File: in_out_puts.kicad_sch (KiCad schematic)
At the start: 16 parts, among them J2 Status_leds, J3 Dome, J5 Motor1, J6 Motor2, J7 Speaker, Q4 PNP, Q5 NMOS, Q6 NMOS, SW2 SW_Push, SW3 SW_Push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

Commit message: simulated IR-constant-current circuit, worked on schematic
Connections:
- net IO42: now reaches Q6.2 (G)
- net IO41: now reaches Q5.2 (G)
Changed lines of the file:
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@@
+		)
+	)
+	(global_label "IO41"
+		(shape input)
+		(at 35.56 127 180)
+		(fields_autoplaced yes)
+		(effects
+			(font
+				(size 1.27 1.27)
+			)
+			(justify right)
+		)
+		(property "Intersheetrefs" "${INTERSHEET_REFS}"
+			(at 28.2205 127 0)
+			(effects
+				(font
+					(size 1.27 1.27)
+				)
+				(justify right)
+				(hide yes)
+			)
 		)
 	)
@@
 			(effects
 				(font
+					(size 1.27 1.27)
+				)
+				(justify right)
+				(hide yes)
+			)
+		)
+	)
+	(global_label "IO42"
+		(shape input)
+		(at 64.77 127 180)
+		(fields_autoplaced yes)
+		(effects
+			(font
+				(size 1.27 1.27)
+			)
+			(justify right)
+		)
+		(property "Intersheetrefs" "${INTERSHEET_REFS}"
+			(at 57.4305 127 0)
+			(effects
+				(font

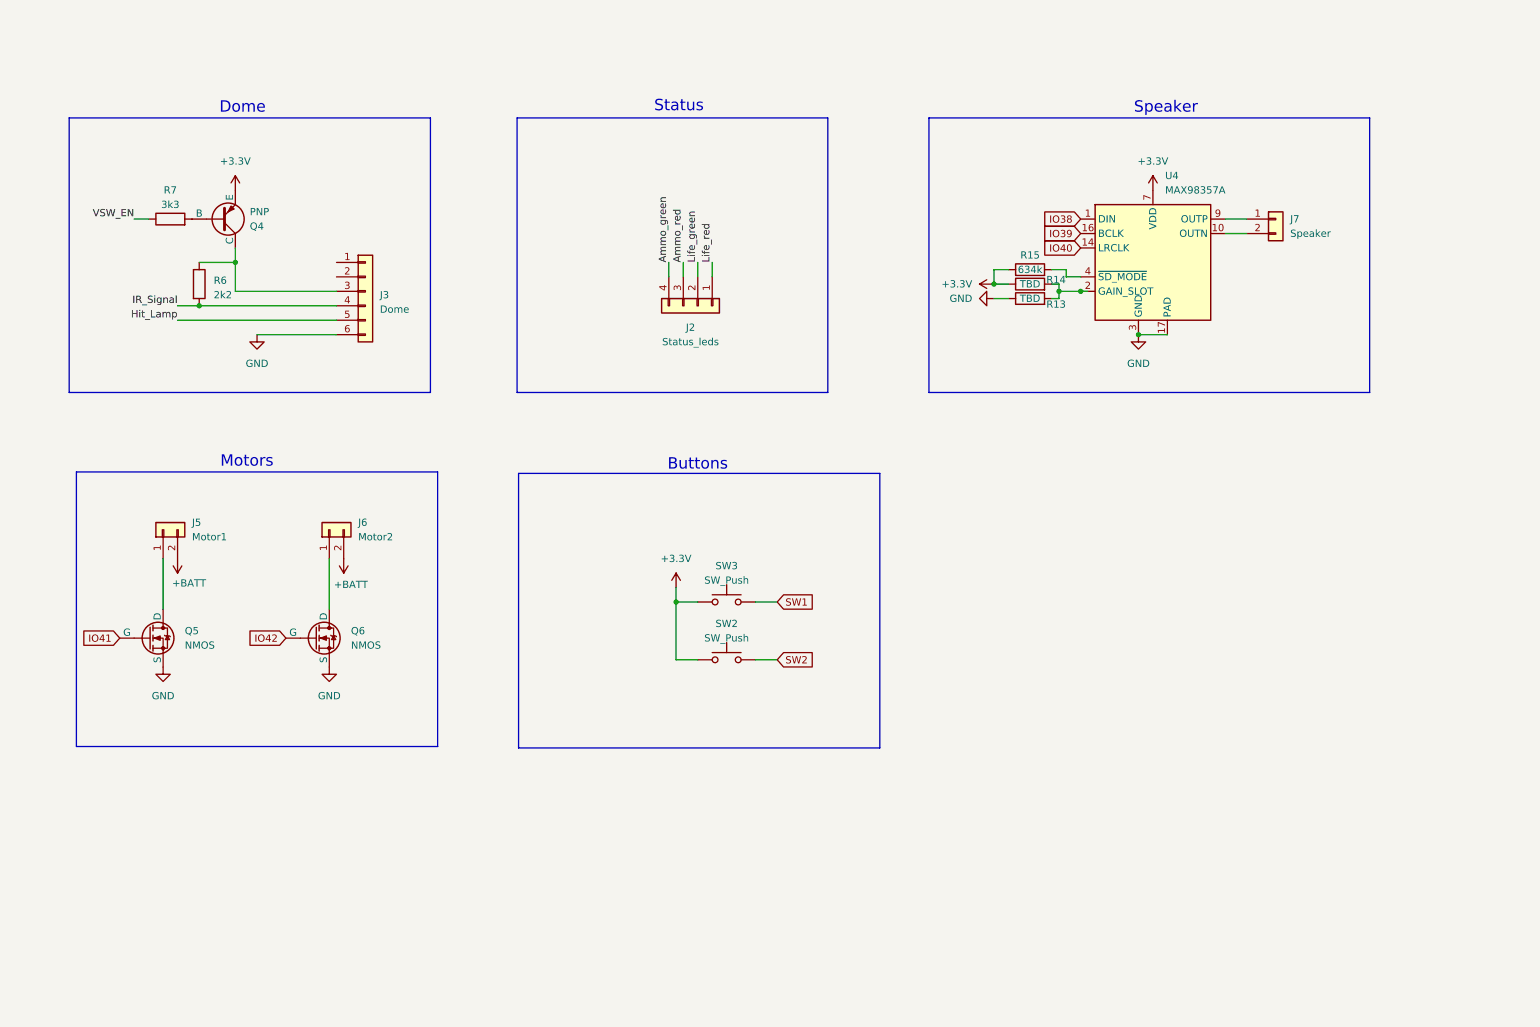
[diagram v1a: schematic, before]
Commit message: prepared for jlcpcb ordering.
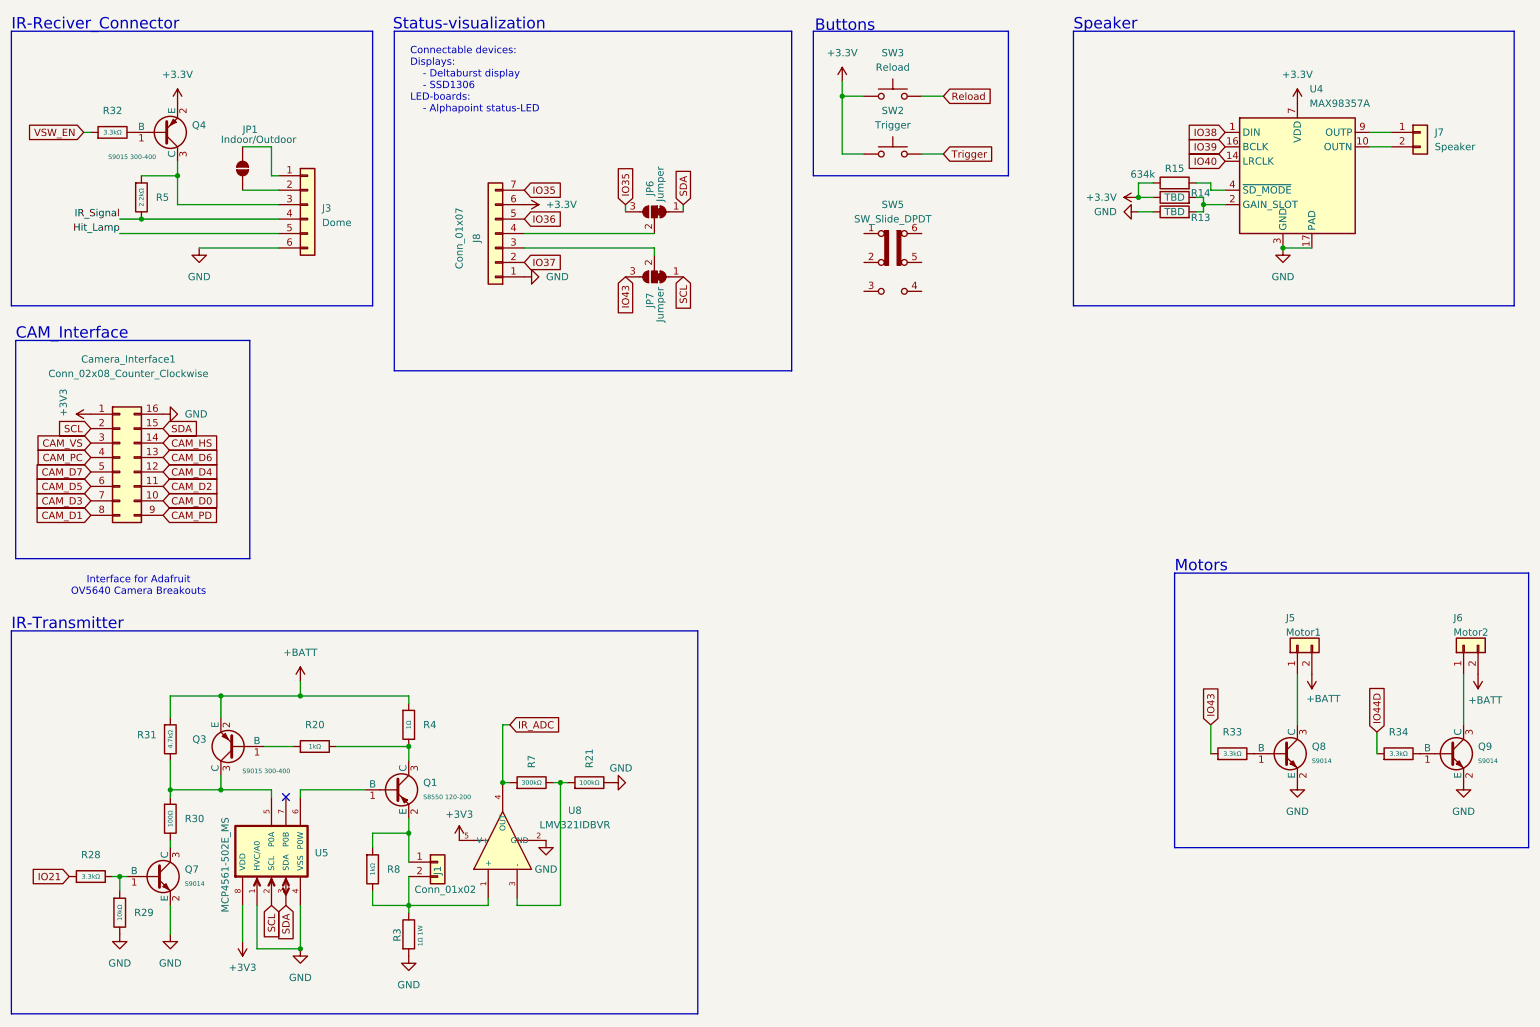
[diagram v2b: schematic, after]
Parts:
- removed J2: Status_leds, symbol Connector_Generic:Conn_01x04
- removed Q4: PNP, symbol Simulation_SPICE:PNP
- removed Q5, Q6: NMOS, symbol Simulation_SPICE:NMOS
- removed R6: 2k2, symbol Device:R
- removed R7: 3k3, symbol Device:R
- added Camera_Interface1: Conn_02x08_Counter_Clockwise, symbol Connector_Generic:Conn_02x08_Counter_Clockwise
- added J1: Conn_01x02, symbol Connector_Generic:Conn_01x02
- added J8: Conn_01x07, symbol Connector_Generic:Conn_01x07
- added JP1: Indoor/Outdoor, symbol Jumper:SolderJumper_2_Open
- added JP6, JP7: Jumper, symbol Jumper:SolderJumper_3_Bridged12
- added Q1: S8550 120-200, PCM_JLCPCB:Q_SOT-23, symbol PCM_JLCPCB-Transistors:PNP,S8550 120-200
- added Q3, Q4: S9015 300-400, PCM_JLCPCB:Q_SOT-23, symbol PCM_JLCPCB-Transistors:PNP,S9015 300-400
- added Q7, Q8, Q9: S9014, PCM_JLCPCB:Q_SOT-23, symbol PCM_JLCPCB-Transistors:NPN,S9014
- added R20, R8: 1kΩ, PCM_JLCPCB:R_0603, symbol PCM_JLCPCB-Resistors:0603,1kΩ
- added R21: 100kΩ, PCM_JLCPCB:R_0603, symbol PCM_JLCPCB-Resistors:0603,100kΩ
- added R28, R32, R33, R34: 3.3kΩ, PCM_JLCPCB:R_0603, symbol PCM_JLCPCB-Resistors:0603,3.3kΩ
- added R29: 10kΩ, PCM_JLCPCB:R_0603, symbol PCM_JLCPCB-Resistors:0603,10kΩ
- added R3: 1Ω 1W, symbol Device:R
- added R30: 100Ω, PCM_JLCPCB:R_0603, symbol PCM_JLCPCB-Resistors:0603,100Ω
- added R31: 4.7kΩ, PCM_JLCPCB:R_0603, symbol PCM_JLCPCB-Resistors:0603,4.7kΩ
- added R4: 1Ω, PCM_JLCPCB:R_0603, symbol PCM_JLCPCB-Resistors:0603,1Ω
- added R5: 2.2kΩ, PCM_JLCPCB:R_0603, symbol PCM_JLCPCB-Resistors:0603,2.2kΩ
- added R7: 300kΩ, PCM_JLCPCB:R_0603, symbol PCM_JLCPCB-Resistors:0603,300kΩ
- added SW5: SW_Slide_DPDT, symbol Switch:SW_Slide_DPDT
- added U5: MCP4561-502E_MS, MCP4561-502E_MS:SOP65P490X110-8N, symbol MCP4561-502E_MS:MCP4561-502E_MS
- added U8: LMV321IDBVR, PCM_JLCPCB:SOT-23-5_L3.0-W1.7-P0.95-LS2.8-BR, symbol PCM_JLCPCB-Analog:Op-Amp, LMV321IDBVR
- SW2: value SW_Push -> Trigger
- SW3: value SW_Push -> Reload
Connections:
- net +3.3V: now also J8.6 (Pin_6), Q4.2 (E)
- net +BATT: now also Q3.2 (E), R31.1, R4.1
- net GND: now also Camera_Interface1.16 (Pin_16), J8.1 (Pin_1), Q7.2 (E), Q8.2 (E), Q9.2 (E), R21.2, R29.2, R3.2, U5.1 (HVC/A0), U5.4 (VSS), U8.2 (GND)
- net IR_Signal: now also R5.2
- net VSW_EN: now also R32.1
- net at J6.1 (Pin_1): now also Q9.3 (C)
- net at J5.1 (Pin_1): now also Q8.3 (C)
- net at J3.3 (Pin_3): now also Q4.3 (C), R5.1
- net at J3.1 (Pin_1): now also JP1.2 (B)
- net at J3.2 (Pin_2): now also JP1.1 (A)
- net SW1 renamed Reload
- net SW2 renamed Trigger
- new net: J1.2 (Pin_2), R3.1, R8.2, U8.1 (+)
- new net: Q7.1 (B), R28.2, R29.1
- new net: J8.3 (Pin_3), JP7.2 (C)
- new net: Q9.1 (B), R34.2
- new net: Q3.1 (B), R20.1
- new net: Q3.3 (C), R30.1, R31.2, U5.5 (P0A)
- new net: Q8.1 (B), R33.2
- new net: J1.1 (Pin_1), Q1.2 (E), R8.1
- new net: R21.1, R7.2, U8.3 (-)
- new net: J8.4 (Pin_4), JP6.2 (C)
- new net: Q1.1 (B), U5.6 (P0W)
- new net: Q1.3 (C), R20.2, R4.2
- new net: Q7.3 (C), R30.2
- new net: Q4.1 (B), R32.2
- new net +3V3: Camera_Interface1.1 (Pin_1), U5.8 (VDD), U8.5 (V+)
- new net CAM_D0: Camera_Interface1.10 (Pin_10)
- new net CAM_D1: Camera_Interface1.8 (Pin_8)
- new net CAM_D2: Camera_Interface1.11 (Pin_11)
- new net CAM_D3: Camera_Interface1.7 (Pin_7)
- new net CAM_D4: Camera_Interface1.12 (Pin_12)
- new net CAM_D5: Camera_Interface1.6 (Pin_6)
- new net CAM_D6: Camera_Interface1.13 (Pin_13)
- new net CAM_D7: Camera_Interface1.5 (Pin_5)
- new net CAM_HS: Camera_Interface1.14 (Pin_14)
- new net CAM_PC: Camera_Interface1.4 (Pin_4)
- new net CAM_PD: Camera_Interface1.9 (Pin_9)
- new net CAM_VS: Camera_Interface1.3 (Pin_3)
- new net IO21: R28.1
- new net IO35: J8.7 (Pin_7), JP6.3 (B)
- new net IO36: J8.5 (Pin_5)
- new net IO37: J8.2 (Pin_2)
- new net IO43: JP7.3 (B), R33.1
- new net IO44D: R34.1
- new net IR_ADC: R7.1, U8.4 (OUT)
- new net SCL: Camera_Interface1.2 (Pin_2), JP7.1 (A), U5.2 (SCL)
- new net SDA: Camera_Interface1.15 (Pin_15), JP6.1 (A), U5.3 (SDA)
- no-connect marks 0 -> 1
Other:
- note added: "CAM_Interface"
- note added: "Connectable devices: Displays: - Deltaburst display - SSD1306 LED-boards: - Alphapoint status-LED"
- note added: "IR-Reciver_Connector"
- note added: "IR-Transmitter"
- note added: "Interface for Adafruit OV5640 Camera Breakouts"
- note added: "Status-visualization"
- note removed: "Dome"
- note removed: "Status"
- moved on the sheet: J3, J5, J6, J7, R13, R14, R15, SW2, SW3, U4

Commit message: checked and fixed schematic, analized it with traceformer.io ai
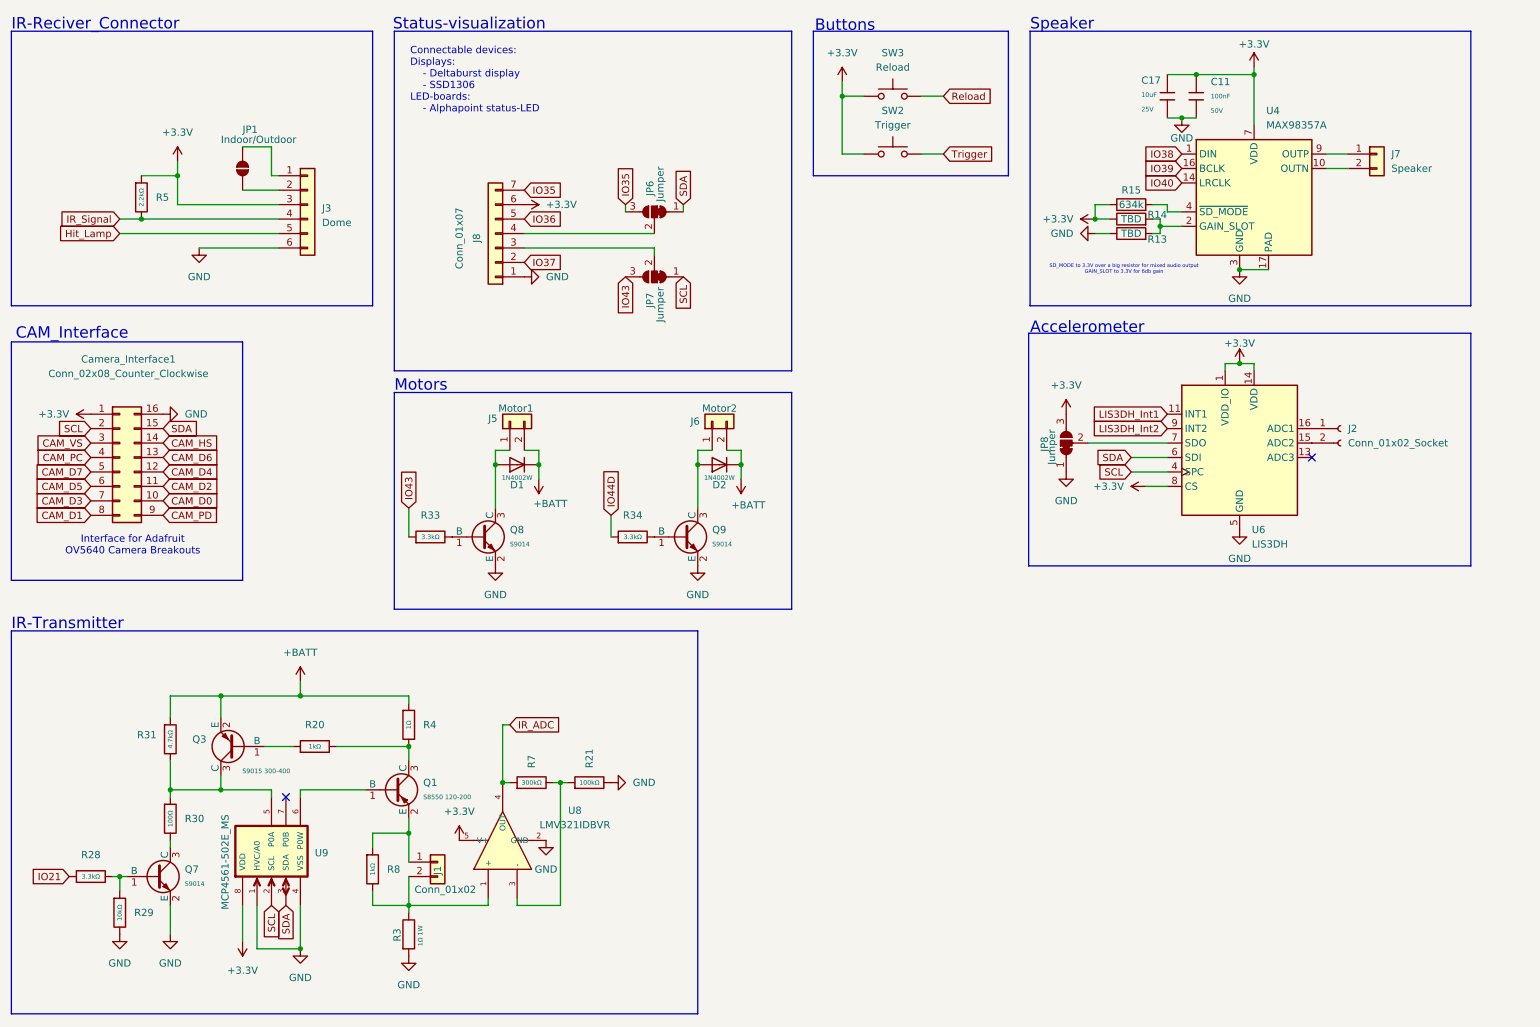
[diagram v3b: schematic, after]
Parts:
- removed Q4: S9015 300-400, PCM_JLCPCB:Q_SOT-23, symbol PCM_JLCPCB-Transistors:PNP,S9015 300-400
- removed R32: 3.3kΩ, PCM_JLCPCB:R_0603, symbol PCM_JLCPCB-Resistors:0603,3.3kΩ
- removed SW5: SW_Slide_DPDT, symbol Switch:SW_Slide_DPDT
- removed U5: MCP4561-502E_MS, MCP4561-502E_MS:SOP65P490X110-8N, symbol MCP4561-502E_MS:MCP4561-502E_MS
- added C11: 100nF, PCM_JLCPCB:C_0603, symbol PCM_JLCPCB-Capacitors:0603,100nF
- added C17: 10uF, PCM_JLCPCB:C_0805, symbol PCM_JLCPCB-Capacitors:0805,10uF
- added D1, D2: 1N4002W, PCM_JLCPCB:D_SOD-123FL, symbol PCM_JLCPCB-Diodes:General,1N4002W
- added J2: Conn_01x02_Socket, Connector_PinHeader_2.54mm:PinHeader_1x02_P2.54mm_Vertical, symbol Connector:Conn_01x02_Socket
- added JP8: Jumper, Jumper:SolderJumper-3_P1.3mm_Bridged12_RoundedPad1.0x1.5mm_NumberLabels, symbol Jumper:SolderJumper_3_Bridged12
- added U6: LIS3DH, Package_LGA:LGA-16_3x3mm_P0.5mm_LayoutBorder3x5y, symbol Sensor_Motion:LIS3DH
- added U9: MCP4561-502E_MS, MCP4561_502E_MS:SOP65P490X110-8N, symbol MCP4561-502E_MS:MCP4561-502E_MS
- Camera_Interface1: footprint (none) -> Connector_PinHeader_2.54mm:PinHeader_2x08_P2.54mm_Vertical
- J1: footprint (none) -> Connector_PinHeader_2.54mm:PinHeader_1x01_P2.54mm_Vertical
- J3: footprint (none) -> Connector_PinHeader_1.00mm:PinHeader_1x06_P1.00mm_Vertical
- J5, J6, J7: footprint (none) -> Connector_PinHeader_1.00mm:PinHeader_1x02_P1.00mm_Vertical
- J8: footprint (none) -> Connector_PinHeader_2.54mm:PinHeader_1x07_P2.54mm_Vertical
- JP1: footprint (none) -> Jumper:SolderJumper-2_P1.3mm_Open_RoundedPad1.0x1.5mm
- JP6, JP7: footprint (none) -> Jumper:SolderJumper-3_P1.3mm_Bridged12_RoundedPad1.0x1.5mm_NumberLabels
- R13, R14, R15: footprint (none) -> Resistor_SMD:R_0805_2012Metric_Pad1.20x1.40mm_HandSolder
- R3: footprint (none) -> Resistor_SMD:R_2512_6332Metric_Pad1.40x3.35mm_HandSolder
- SW2, SW3: footprint (none) -> Connector_PinHeader_1.00mm:PinHeader_1x02_P1.00mm_Horizontal
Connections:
- net +3V3 is gone; now on net +3.3V: Camera_Interface1.1 (Pin_1), U8.5 (V+)
- net +3.3V: now also J3.3 (Pin_3), R5.1, C11.1, C17.1, JP8.3 (B), U6.1 (VDD_IO), U6.14 (VDD), U6.8 (CS), U9.8 (VDD)
- net +BATT: now also D1.1, D2.1
- net GND: now also C11.2, C17.2, JP8.1 (A), U6.10 (GND), U6.12 (GND), U6.5 (GND), U9.1 (HVC/A0), U9.4 (VSS)
- net SCL: now also U6.4 (SPC), U9.2 (SCL)
- net SDA: now also U6.6 (SDI), U9.3 (SDA)
- net at J6.1 (Pin_1), Q9.3 (C): now also D2.2
- net at Q3.3 (C), R30.1, R31.2: now also U9.5 (P0A)
- net at J5.1 (Pin_1), Q8.3 (C): now also D1.2
- net at Q1.1 (B): now also U9.6 (P0W)
- new net: J2.1 (Pin_1), U6.16 (ADC1)
- new net: J2.2 (Pin_2), U6.15 (ADC2)
- new net: JP8.2 (C), U6.7 (SDO)
- new net LIS3DH_Int1: U6.11 (INT1)
- new net LIS3DH_Int2: U6.9 (INT2)
- no-connect marks 1 -> 2
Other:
- note added: "Accelerometer"
- note added: "SD_MODE to 3.3V over a big resistor for mixed audio output GAIN_SLOT to 3.3V for 6db gain"
- moved on the sheet: J5, J6, J7, Q8, Q9, R13, R14, R15, R33, R34, U4

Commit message: replaced ir-led constant current circuit
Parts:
- removed C11: 100nF, PCM_JLCPCB:C_0603, symbol PCM_JLCPCB-Capacitors:0603,100nF
- removed Q1: S8550 120-200, PCM_JLCPCB:Q_SOT-23, symbol PCM_JLCPCB-Transistors:PNP,S8550 120-200
- removed Q3: S9015 300-400, PCM_JLCPCB:Q_SOT-23, symbol PCM_JLCPCB-Transistors:PNP,S9015 300-400
- removed Q7: S9014, PCM_JLCPCB:Q_SOT-23, symbol PCM_JLCPCB-Transistors:NPN,S9014
- removed R20, R8: 1kΩ, PCM_JLCPCB:R_0603, symbol PCM_JLCPCB-Resistors:0603,1kΩ
- removed R21: 100kΩ, PCM_JLCPCB:R_0603, symbol PCM_JLCPCB-Resistors:0603,100kΩ
- removed R28, R33, R34: 3.3kΩ, PCM_JLCPCB:R_0603, symbol PCM_JLCPCB-Resistors:0603,3.3kΩ
- removed R29: 10kΩ, PCM_JLCPCB:R_0603, symbol PCM_JLCPCB-Resistors:0603,10kΩ
- removed R30: 100Ω, PCM_JLCPCB:R_0603, symbol PCM_JLCPCB-Resistors:0603,100Ω
- removed R31: 4.7kΩ, PCM_JLCPCB:R_0603, symbol PCM_JLCPCB-Resistors:0603,4.7kΩ
- removed R4: 1Ω, PCM_JLCPCB:R_0603, symbol PCM_JLCPCB-Resistors:0603,1Ω
- removed R5: 2.2kΩ, PCM_JLCPCB:R_0603, symbol PCM_JLCPCB-Resistors:0603,2.2kΩ
- removed R7: 300kΩ, PCM_JLCPCB:R_0603, symbol PCM_JLCPCB-Resistors:0603,300kΩ
- removed U9: MCP4561-502E_MS, MCP4561_502E_MS:SOP65P490X110-8N, symbol MCP4561-502E_MS:MCP4561-502E_MS
- added C10, C28: 100nF, PCM_JLCPCB:C_0805, symbol PCM_JLCPCB-Capacitors:0805,100nF,(2)
- added C27: 22pF, PCM_JLCPCB:C_0805, symbol PCM_JLCPCB-Capacitors:0805,22pF
- added C29: 10uF, PCM_JLCPCB:C_0805, symbol PCM_JLCPCB-Capacitors:0805,10uF
- added Q1: IRLML6344TRPBF, IRLML6344TRPBF:TRANS_IRLML6344TRPBF, symbol IRLML6344TRPBF:IRLML6344TRPBF
- added R20: 100Ω, PCM_JLCPCB:R_0805, symbol PCM_JLCPCB-Resistors:0805,100Ω
- added R21: 150kΩ, PCM_JLCPCB:R_0805, symbol PCM_JLCPCB-Resistors:0805,150kΩ
- added R23, R24: 3.3kΩ, PCM_JLCPCB:R_0805, symbol PCM_JLCPCB-Resistors:0805,3.3kΩ
- added R4: 100kΩ, PCM_JLCPCB:R_0805, symbol PCM_JLCPCB-Resistors:0805,100kΩ
- added R5: 2.2kΩ, PCM_JLCPCB:R_0805, symbol PCM_JLCPCB-Resistors:0805,2.2kΩ
- added R7: 1.5kΩ, PCM_JLCPCB:R_0805, symbol PCM_JLCPCB-Resistors:0805,1.5kΩ
- added R8: 750Ω, PCM_JLCPCB:R_0805, symbol PCM_JLCPCB-Resistors:0805,750Ω
- added U5: MCP4531T-103E_MS, MCP4561_103E_MS:SOP65P490X110-8N, symbol MCP4531T-103E_MS:MCP4531T-103E_MS
- added U9: OPA197IDR, opa197idr:D0008A-IPC_A, symbol 2026-02-26_14-50-16:OPA197IDR
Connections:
- net +3.3V: now also C28.1, R5.1, U5.8 (VDD)
- net +BATT: now also J1.1 (Pin_1), C10.1, C29.1, U9.7 (V+)
- net GND: now also C10.2, C28.2, C29.2, R4.2, R8.2, U5.1 (HVC/A0), U5.4 (VSS), U9.4 (V-)
- net IO21: now also U5.6 (P0W)
- net IO43: now also R23.1
- net IO44D: now also R24.1
- net IR_ADC: now also R21.1
- net IR_Signal: now also R5.2
- net SCL: now also U5.2 (SCL)
- net SDA: now also U5.3 (SDA)
- net at R3.1, U8.1 (+): now also C27.2, Q1.2, U9.2 (-IN); no longer J1.2 (Pin_2)
- net at Q9.1 (B): now also R24.2
- net at Q8.1 (B): now also R23.2
- net at U8.3 (-): now also R21.2, R4.1
- new net: C27.1, R20.1, U9.6 (OUT)
- new net: Q1.1, R20.2
- new net: R7.2, R8.1, U9.3 (+IN)
- new net: R7.1, U5.5 (P0A)
- new net: J1.2 (Pin_2), Q1.3
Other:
- moved on the sheet: J1, R3, U8

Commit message: pcb layout designing
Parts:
- removed J1: Conn_01x02, Connector_PinHeader_2.54mm:PinHeader_1x01_P2.54mm_Vertical, symbol Connector_Generic:Conn_01x02
- removed R13, R14: TBD, Resistor_SMD:R_0805_2012Metric_Pad1.20x1.40mm_HandSolder, symbol Device:R
- added C30, C32: 10uF, PCM_JLCPCB:C_0805, symbol PCM_JLCPCB-Capacitors:0805,10uF
- added C31, C33: 100nF, PCM_JLCPCB:C_0805, symbol PCM_JLCPCB-Capacitors:0805,100nF,(2)
- added J9: IR-LED, Connector_PinHeader_2.54mm:PinHeader_1x02_P2.54mm_Vertical, symbol Connector_Generic:Conn_01x02
- added R27, R28: 0Ω, PCM_JLCPCB:R_0805, symbol PCM_JLCPCB-Resistors:0805,0Ω
- Camera_Interface1: footprint Connector_PinHeader_2.54mm:PinHeader_2x08_P2.54mm_Vertical -> Connector_JST:JST_PH_B16B-PH-SM4-TB_1x16-1MP_P2.00mm_Vertical
- J3: footprint Connector_PinHeader_1.00mm:PinHeader_1x06_P1.00mm_Vertical -> Connector_JST:JST_PH_S6B-PH-SM4-TB_1x06-1MP_P2.00mm_Horizontal
- J5, J6, J7: footprint Connector_PinHeader_1.00mm:PinHeader_1x02_P1.00mm_Vertical -> Connector_JST:JST_PH_S2B-PH-SM4-TB_1x02-1MP_P2.00mm_Horizontal
- J8: footprint Connector_PinHeader_2.54mm:PinHeader_1x07_P2.54mm_Vertical -> Connector_JST:JST_PH_S7B-PH-SM4-TB_1x07-1MP_P2.00mm_Horizontal
- SW2, SW3: footprint Connector_PinHeader_1.00mm:PinHeader_1x02_P1.00mm_Horizontal -> Connector_PinHeader_2.54mm:PinHeader_1x02_P2.54mm_Vertical
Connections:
- net +3.3V: now also C30.1, C31.1, C32.1, C33.1, R27.1
- net +BATT: now also J9.1 (Pin_1)
- net GND: now also C30.2, C31.2, C32.2, C33.2, R28.1
- net at U4.2 (GAIN_SLOT): now also R27.2, R28.2
- net at Q1.3: now also J9.2 (Pin_2)
